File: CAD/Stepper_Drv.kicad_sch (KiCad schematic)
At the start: 16 parts, among them U1 SN74F125DR, U2 SN74F125DR, U21 SN74F125DR, U22 SN74F125DR, U24 SN74F125DR, U31 74LVC06A, U32 74LVC06A, U6 74LVC06A

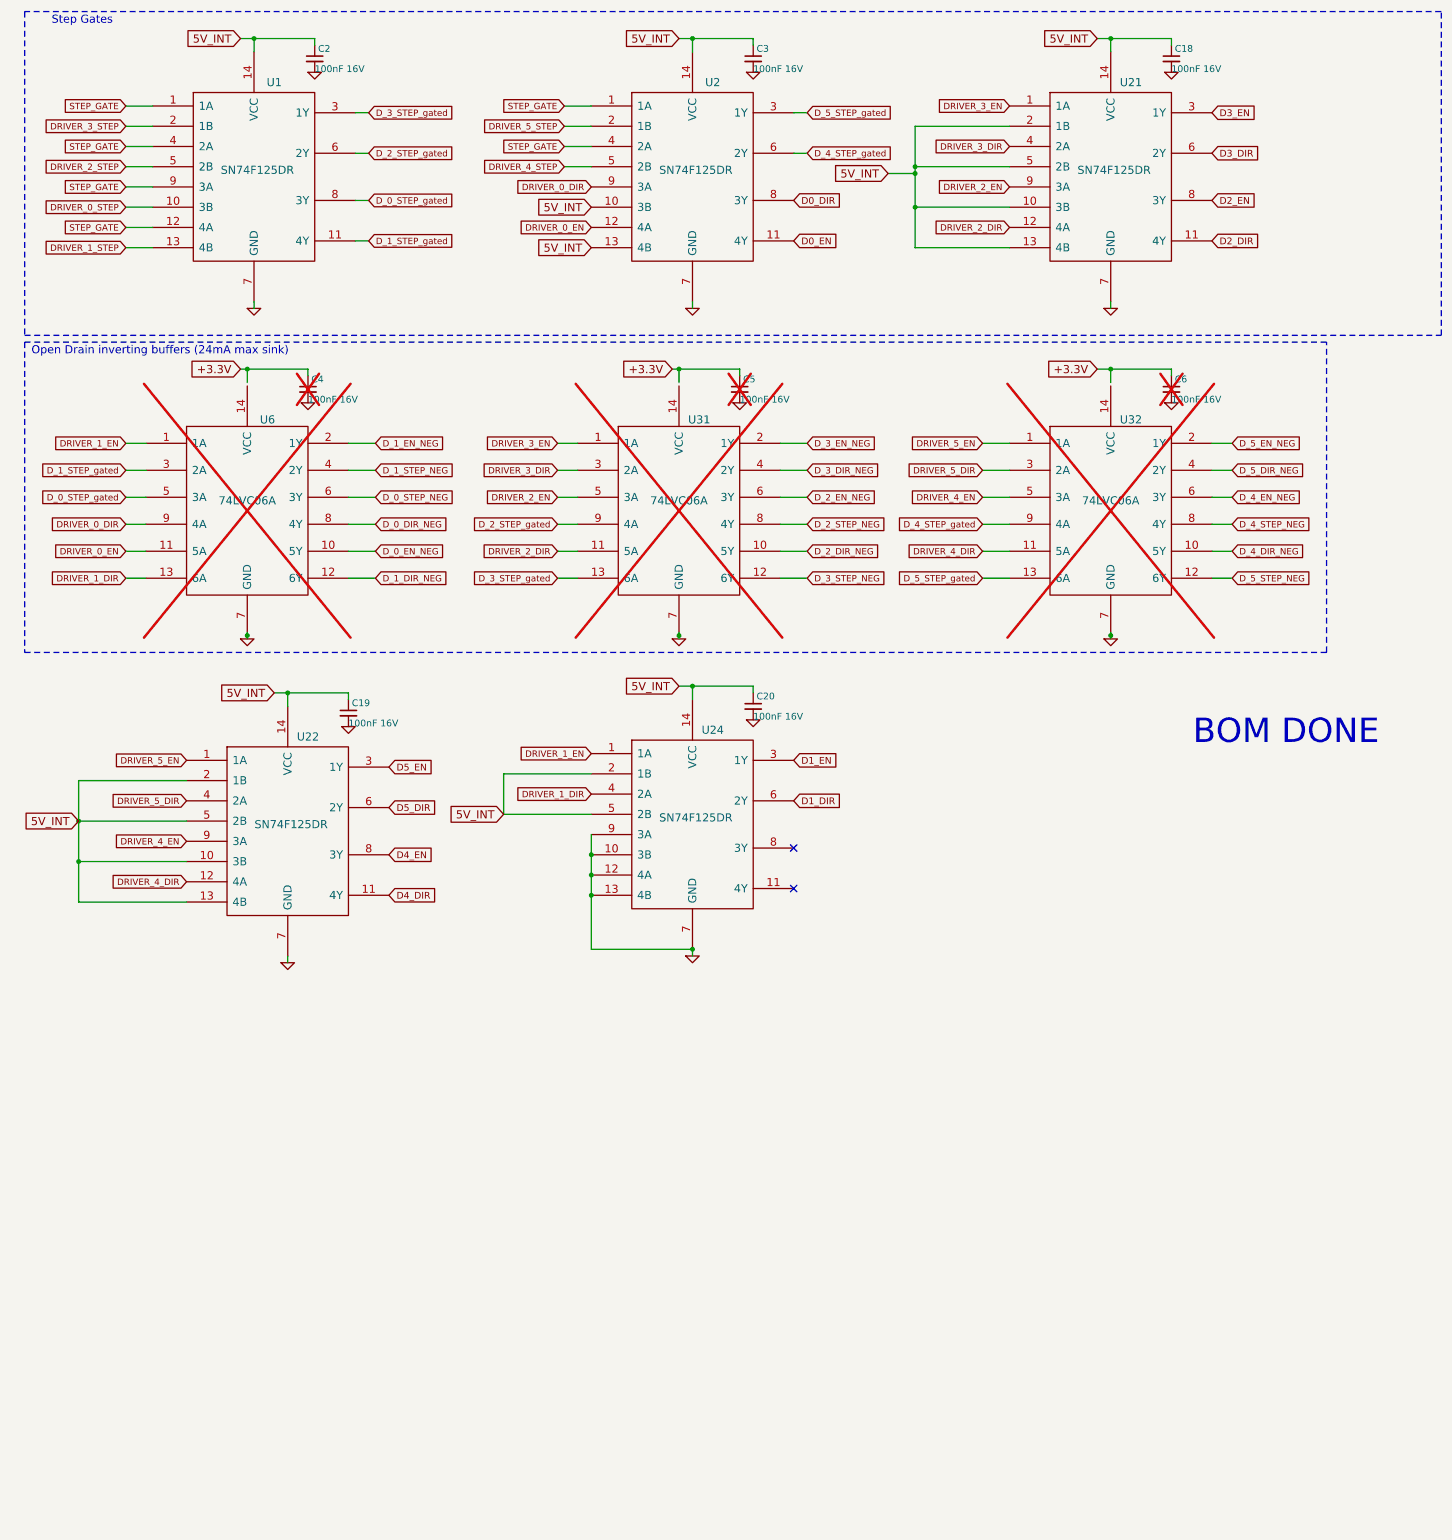
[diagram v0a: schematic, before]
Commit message: WIP redoing board for new print
Removed version resistors.
Added pull-up on CMD.
Working on motors, not routed.
Added local library for custom parts.
Ran auto-cleanup of traces and vias (supervised).
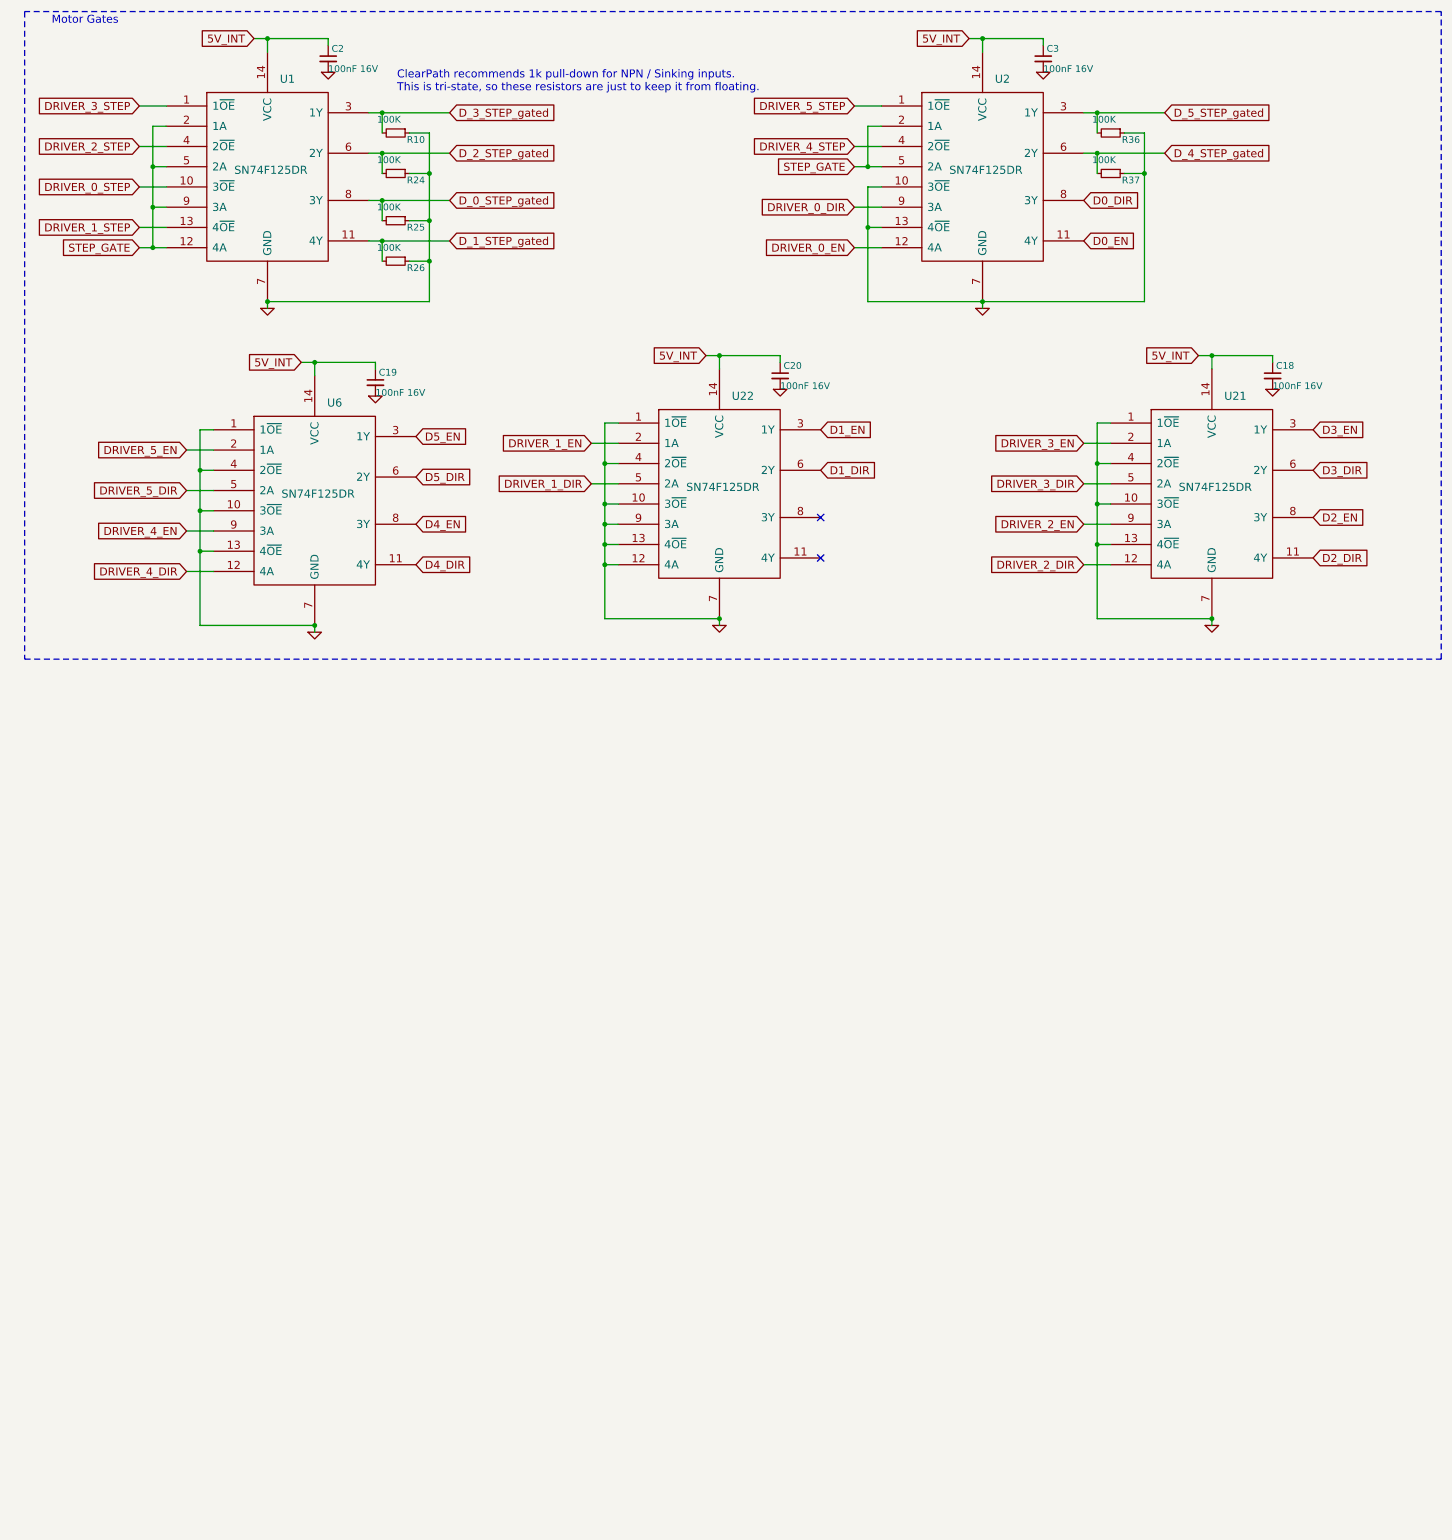
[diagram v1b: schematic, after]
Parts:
- removed C4, C5, C6: 100nF 16V, Capacitor_SMD:C_0402_1005Metric_Wbry, symbol Device:C_Small
- removed U1, U2, U21, U22, U24: SN74F125DR, Package_SO:SOIC-14_3.9x8.7mm_P1.27mm, symbol Duet3:74HC08
- removed U31, U32, U6: 74LVC06A, Package_SO:TSSOP-14_4.4x5mm_P0.65mm, symbol Duet3:74LVC06A
- added R10, R24, R25, R26, R36, R37: 100K, Resistor_SMD:R_0402_1005Metric, symbol Device:R_Small
- added U1, U2, U21, U22, U6: SN74F125DR, Package_SO:SOIC-14_3.9x8.7mm_P1.27mm, symbol 3DPotter:SN74F125DR
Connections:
- net 5V_INT: now also U1.14 (VCC), U2.14 (VCC), U21.14 (VCC), U22.14 (VCC), U6.14 (VCC)
- net D0_DIR: now also U2.8 (3Y)
- net D0_EN: now also U2.11 (4Y)
- net D1_DIR: now also U22.6 (2Y)
- net D1_EN: now also U22.3 (1Y)
- net D2_DIR: now also U21.11 (4Y)
- net D2_EN: now also U21.8 (3Y)
- net D3_DIR: now also U21.6 (2Y)
- net D3_EN: now also U21.3 (1Y)
- net D4_DIR: now also U6.11 (4Y)
- net D4_EN: now also U6.8 (3Y)
- net D5_DIR: now also U6.6 (2Y)
- net D5_EN: now also U6.3 (1Y)
- net DRIVER_0_DIR: now also U2.9 (3A)
- net DRIVER_0_EN: now also U2.12 (4A)
- net DRIVER_0_STEP: now also U1.10 (3~{OE})
- net DRIVER_1_DIR: now also U22.5 (2A)
- net DRIVER_1_EN: now also U22.2 (1A)
- net DRIVER_1_STEP: now also U1.13 (4~{OE})
- net DRIVER_2_DIR: now also U21.12 (4A)
- net DRIVER_2_EN: now also U21.9 (3A)
- net DRIVER_2_STEP: now also U1.4 (2~{OE})
- net DRIVER_3_DIR: now also U21.5 (2A)
- net DRIVER_3_EN: now also U21.2 (1A)
- net DRIVER_3_STEP: now also U1.1 (1~{OE})
- net DRIVER_4_DIR: now also U6.12 (4A)
- net DRIVER_4_EN: now also U6.9 (3A)
- net DRIVER_4_STEP: now also U2.4 (2~{OE})
- net DRIVER_5_DIR: now also U6.5 (2A)
- net DRIVER_5_EN: now also U6.2 (1A)
- net DRIVER_5_STEP: now also U2.1 (1~{OE})
- net D_0_STEP_gated: now also R25.2, U1.8 (3Y)
- net D_1_STEP_gated: now also R26.2, U1.11 (4Y)
- net D_2_STEP_gated: now also R24.2, U1.6 (2Y)
- net D_3_STEP_gated: now also R10.2, U1.3 (1Y)
- net D_4_STEP_gated: now also R37.2, U2.6 (2Y)
- net D_5_STEP_gated: now also R36.2, U2.3 (1Y)
- net GND: now also R10.1, R24.1, R25.1, R26.1, R36.1, R37.1, U1.7 (GND), U2.10 (3~{OE}), U2.13 (4~{OE}), U2.7 (GND), U21.1 (1~{OE}), U21.10 (3~{OE}), U21.13 (4~{OE}), U21.4 (2~{OE}), U21.7 (GND), U22.1 (1~{OE}), U22.10 (3~{OE}), U22.12 (4A), U22.13 (4~{OE}), U22.4 (2~{OE}), U22.7 (GND), U22.9 (3A), U6.1 (1~{OE}), U6.10 (3~{OE}), U6.13 (4~{OE}), U6.4 (2~{OE}), U6.7 (GND)
- net STEP_GATE: now also U1.12 (4A), U1.2 (1A), U1.5 (2A), U1.9 (3A), U2.2 (1A), U2.5 (2A)
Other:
- note added: "ClearPath recommends 1k pull-down for NPN / Sinking inputs. This is tri-state, so these resistors are just to keep it from floating."
- note added: "Motor Gates"
- note removed: "BOM DONE"
- note removed: "Open Drain inverting buffers (24mA max sink)"
- note removed: "Step Gates"
- company: Duet3d -> 3DPotter
- title: Duet 3 Main Board 6XD -> Duet 3 Main Board 3DP
- moved on the sheet: C18, C19, C2, C20, C3

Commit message: motors have been routed
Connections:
- net D0_DIR: now also U22.8 (3Y); no longer U2.8 (3Y)
- net D0_EN: now also U22.11 (4Y); no longer U2.11 (4Y)
- net DRIVER_0_DIR: now also U22.9 (3A); no longer U2.9 (3A)
- net DRIVER_0_EN: now also U22.12 (4A); no longer U2.12 (4A)
- net GND: now also U2.12 (4A), U2.9 (3A); no longer U22.12 (4A), U22.9 (3A)
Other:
- moved on the sheet: C18, C20, U21, U22

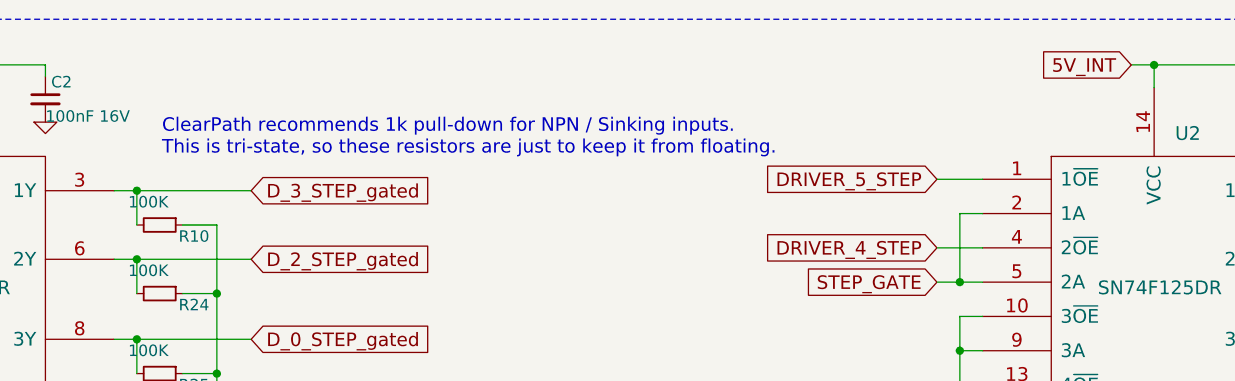
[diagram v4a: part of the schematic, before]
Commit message: QOL
Added a buttload of 3d models, 3d model of board is now usable. Also saved a lot of missing symbols and footprints, which are available in the 3DPotter Library.
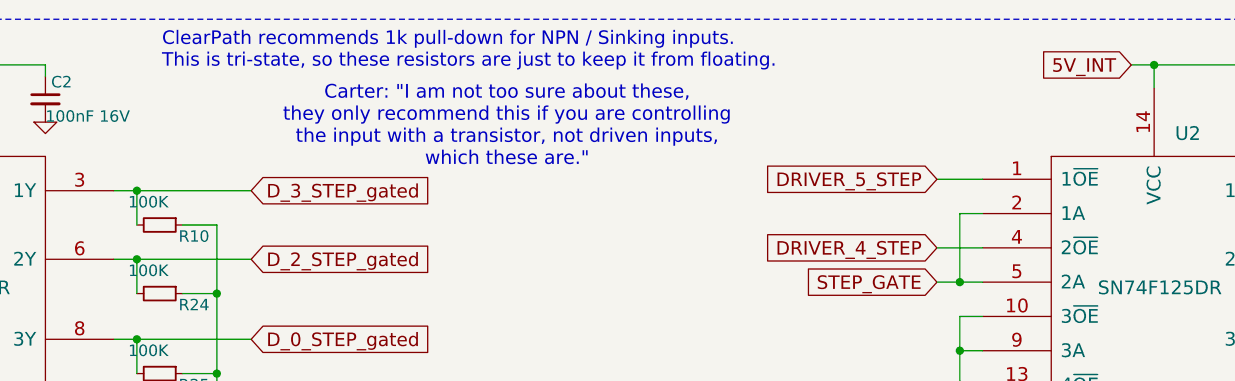
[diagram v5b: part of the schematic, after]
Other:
- note added: "Carter: "I am not too sure about these, they only recommend this if you are controlling the input with a transistor, not driven inputs, which these are.""
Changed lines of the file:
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@@
 		(comment 1 "(c) 3DPotter")
+	)
+	(text "Carter: \"I am not too sure about these, \nthey only recommend this if you are controlling\nthe input with a transistor, not driven inputs,\nwhich these are.\""
+		(exclude_from_sim no)
+		(at 123.698 27.178 0)
+		(effects
+			(font
+				(size 1.524 1.524)
+			)
+		)
 	)
 	(text "Motor Gates"
@@
 	(text "ClearPath recommends 1k pull-down for NPN / Sinking inputs.\nThis is tri-state, so these resistors are just to keep it from floating."
 		(exclude_from_sim no)
-		(at 85.344 30.48 0)
+		(at 85.344 20.828 0)
 		(effects
 			(font
